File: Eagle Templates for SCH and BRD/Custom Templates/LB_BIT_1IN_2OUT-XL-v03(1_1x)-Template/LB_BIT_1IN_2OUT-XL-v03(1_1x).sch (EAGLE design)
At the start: 20 parts, among them U1 LV321SOT23-5, U2 LV321SOT23-5, U3 LV321SOT23-5

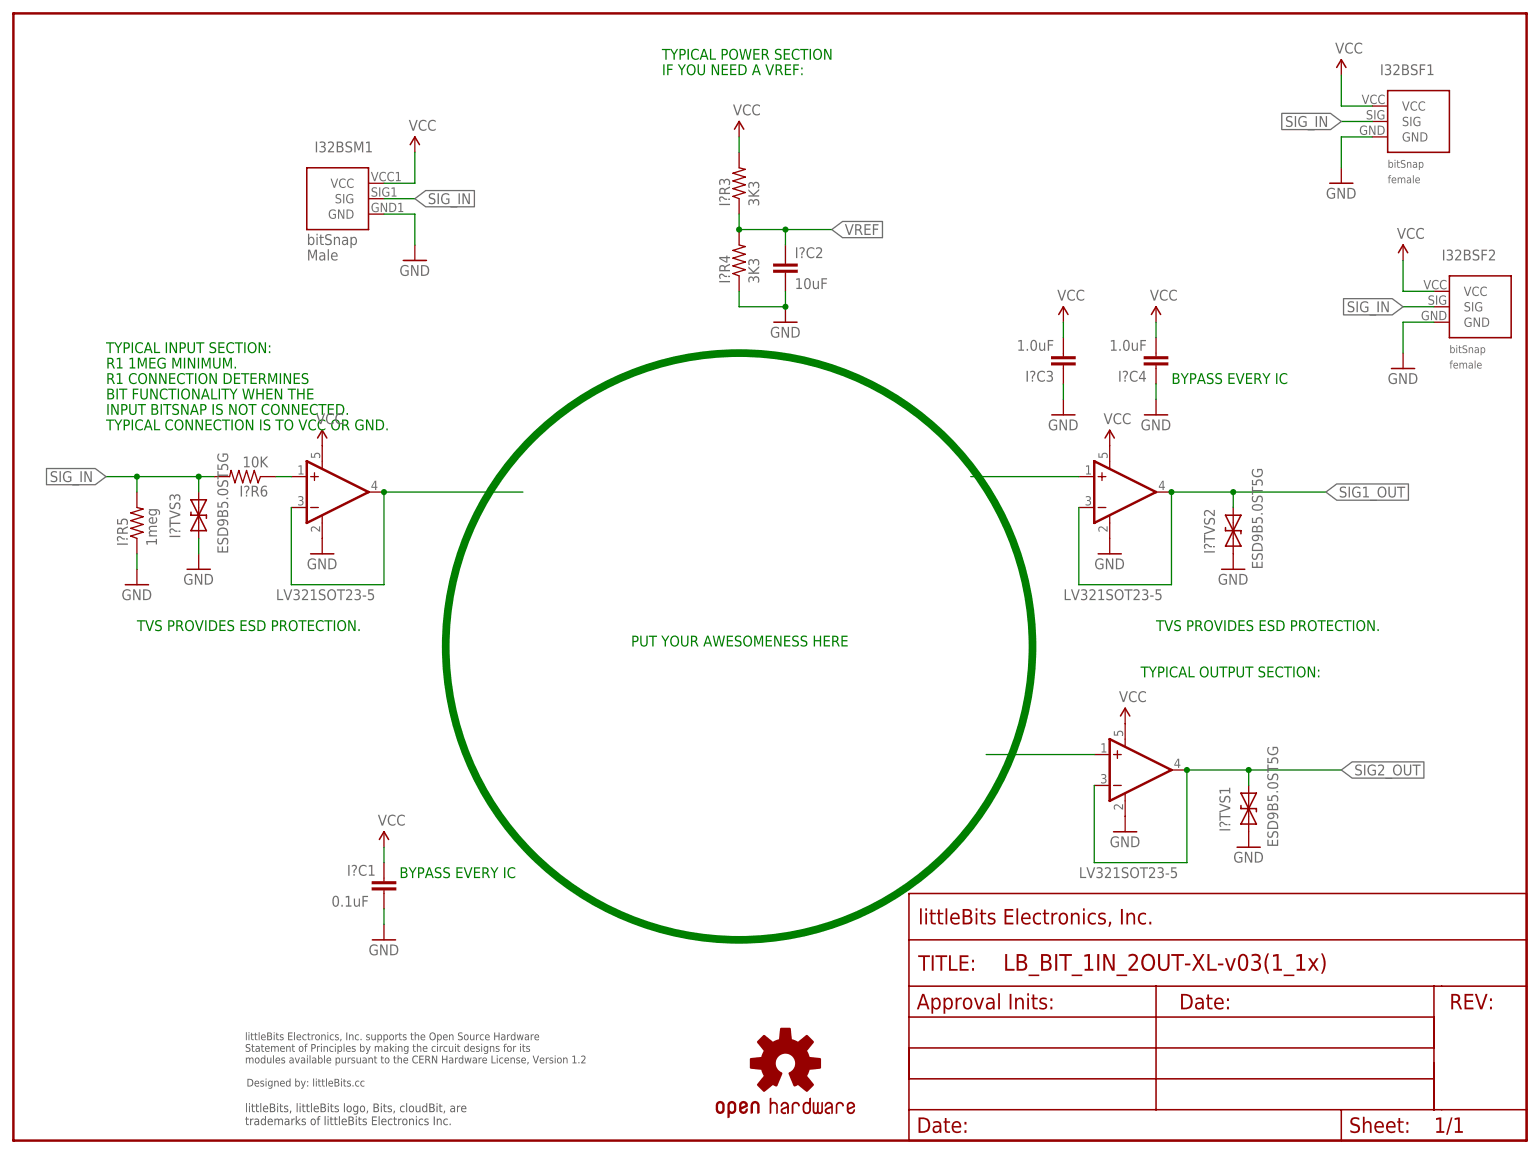
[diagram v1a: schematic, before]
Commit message: Updated templates
- Added ferrite beads
- Moved text and annotations off of Nets layer
- Minor layout changes
- Removed I/O/W prefix from reference designators
- Removed output stage components from output bits
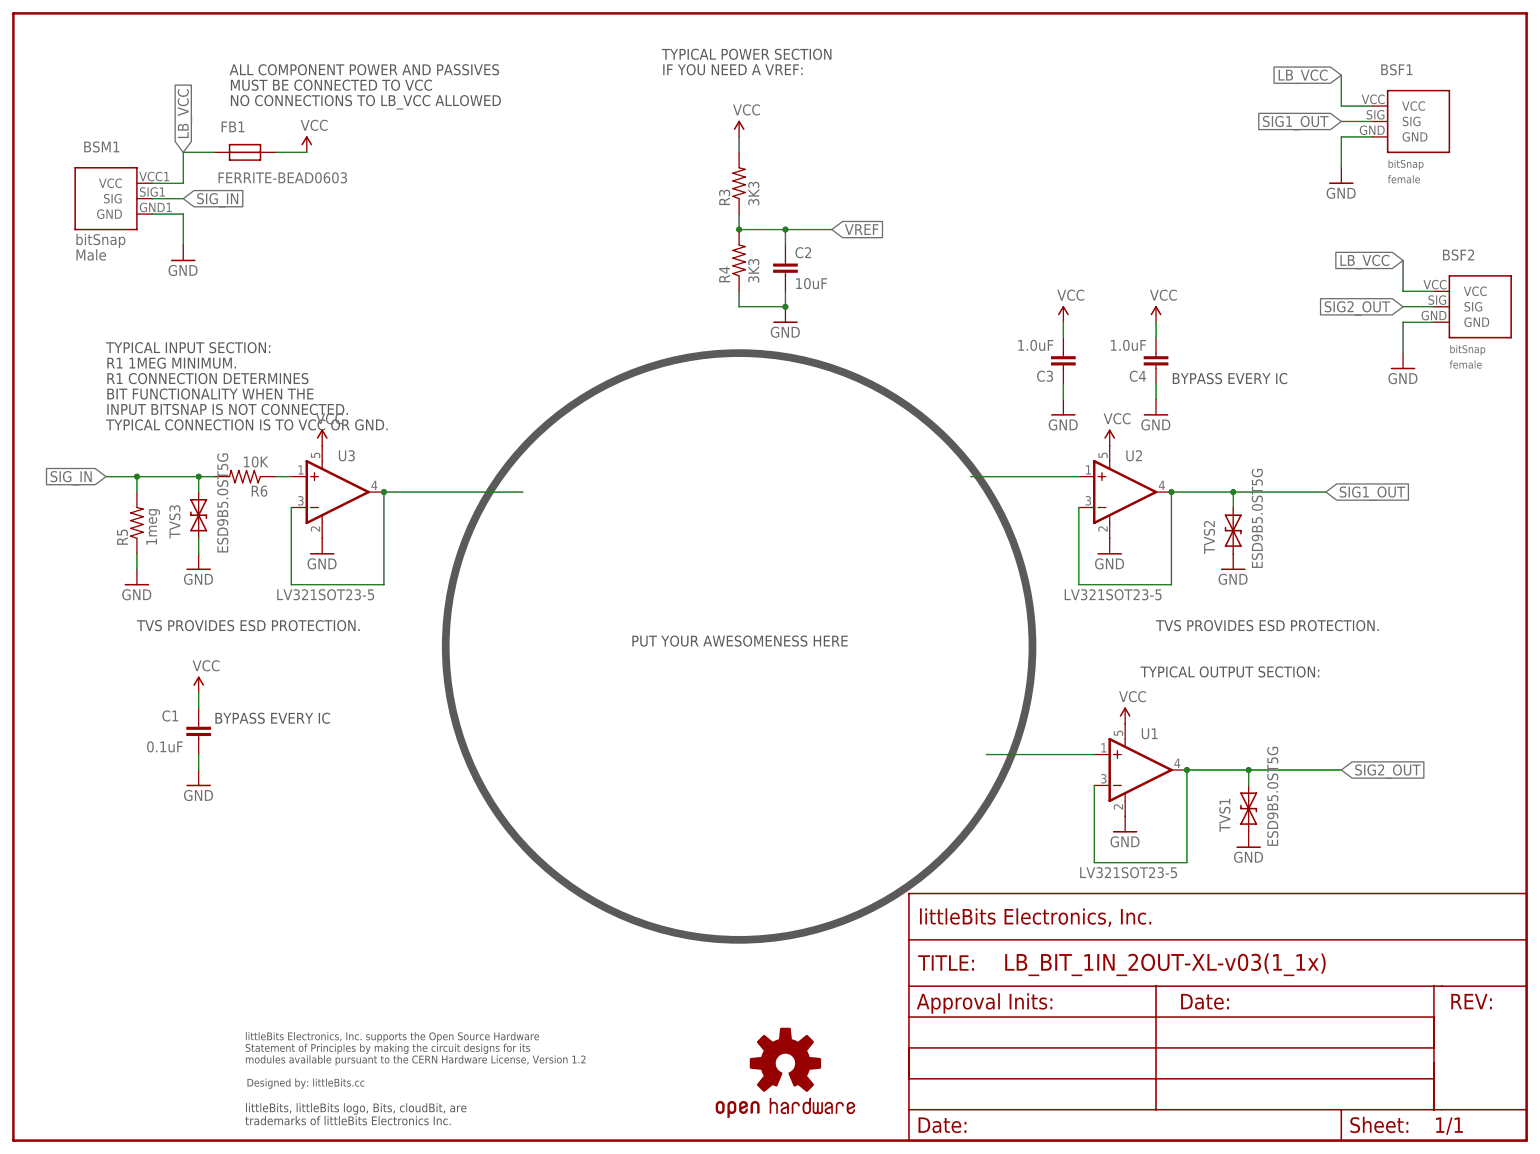
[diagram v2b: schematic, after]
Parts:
- removed I32BSM1: BITSNAP_V03_MALE, bitSnap:BITSNAP_V03_MALE
- removed I?C1: 0.1uF, LITTLEBITS:CAPCAP-0603
- added BSM1: BITSNAP_V03_MALE, bitSnap:BITSNAP_V03_MALE
- added C1: 0.1uF, LITTLEBITS:CAPCAP-0603
- added FB1: FERRITE-BEAD0603, LITTLEBITS:FERRITE-BEAD0603
- renumbered I32BSF1 to BSF1, I32BSF2 to BSF2, I?C2 to C2, I?C3 to C3, I?C4 to C4, I?R3 to R3, I?R4 to R4, I?R5 to R5, I?R6 to R6, I?TVS1 to TVS1, I?TVS2 to TVS2, I?TVS3 to TVS3
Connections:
- new net LB_VCC: BSF1.VCC, BSF2.VCC, BSM1.VCC, FB1.P$2
- net GND: now also BSM1.GND, C1.2; no longer I32BSM1.GND, I?C1.2
- net SIG1_OUT: now also BSF1.SIG
- net SIG2_OUT: now also BSF2.SIG
- net SIG_IN: now also BSM1.SIG; no longer BSF1.SIG, BSF2.SIG, I32BSM1.SIG
- net VCC: now also C1.1, FB1.P$1; no longer BSF1.VCC, BSF2.VCC, I32BSM1.VCC, I?C1.1
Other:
- note added: "ALL COMPONENT POWER AND PASSIVES"
- note added: "MUST BE CONNECTED TO VCC"
- note added: "NO CONNECTIONS TO LB_VCC ALLOWED"
